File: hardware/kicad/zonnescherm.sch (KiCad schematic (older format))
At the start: 28 parts, among them K1 K1-ON/OFF, K2 K1-UP/DOWN, K3 K2-ON/OFF, K4 K2-UP/DOWN, P1 ARDUINO-ISP, P2 CONN_MAINS, P3 CONN_SUNSHADE1, P4 CONN_SUNSHADE2, SW1 SW_UP_1, SW2 SW_DOWN_1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

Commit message: Updated PCB
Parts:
- removed SW1: SW_UP_1, Buttons_Switches_ThroughHole:SW_PUSH_SMALL, symbol SW_PUSH
- removed SW2: SW_DOWN_1, Buttons_Switches_ThroughHole:SW_PUSH_SMALL, symbol SW_PUSH
- removed SW3: SW_UP_2, Buttons_Switches_ThroughHole:SW_PUSH_SMALL, symbol SW_PUSH
- removed SW4: SW_DOWN_2, Buttons_Switches_ThroughHole:SW_PUSH_SMALL, symbol SW_PUSH
- added C5: 100n, Capacitors_SMD:C_0805_HandSoldering, symbol C
- added P5: CONN_02X04, Pin_Headers:Pin_Header_Straight_2x04, symbol CONN_02X04
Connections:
- wire segments 123 -> 134
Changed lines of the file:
@@
-$EndComp
-$Comp
-L SW_PUSH SW1
-U 1 1 57852FF2
-P 1800 4750
-F 0 "SW1" H 1950 4860 50  0000 C CNN
-F 1 "SW_UP_1" H 1800 4670 50  0000 C CNN
-F 2 "Buttons_Switches_ThroughHole:SW_PUSH_SMALL" H 1800 4750 50  0001 C CNN
-F 3 "" H 1800 4750 50  0000 C CNN
-	1    1800 4750
-	1    0    0    -1
-$EndComp
-$Comp
-L SW_PUSH SW2
-U 1 1 57853071
-P 1800 5050
-F 0 "SW2" H 1950 5160 50  0000 C CNN
-F 1 "SW_DOWN_1" H 1800 4970 50  0000 C CNN
-F 2 "Buttons_Switches_ThroughHole:SW_PUSH_SMALL" H 1800 5050 50  0001 C CNN
-F 3 "" H 1800 5050 50  0000 C CNN
-	1    1800 5050
-	1    0    0    -1
-$EndComp
-$Comp
-L SW_PUSH SW3
-U 1 1 57853154
-P 1800 5350
-F 0 "SW3" H 1950 5460 50  0000 C CNN
-F 1 "SW_UP_2" H 1800 5270 50  0000 C CNN
-F 2 "Buttons_Switches_ThroughHole:SW_PUSH_SMALL" H 1800 5350 50  0001 C CNN
-F 3 "" H 1800 5350 50  0000 C CNN
-	1    1800 5350
-	1    0    0    -1
-$EndComp
-$Comp
-L SW_PUSH SW4
-U 1 1 57853197
-P 1800 5650
-F 0 "SW4" H 1950 5760 50  0000 C CNN
-F 1 "SW_DOWN_2" H 1800 5570 50  0000 C CNN
-F 2 "Buttons_Switches_ThroughHole:SW_PUSH_SMALL" H 1800 5650 50  0001 C CNN
-F 3 "" H 1800 5650 50  0000 C CNN
-	1    1800 5650
-	1    0    0    -1
 $EndComp
 $Comp
@@
 XRES
 Wire Wire Line
-	1500 4750 1350 4750
+	1350 4750 1550 4750
 Wire Wire Line
 	1350 4750 1350 5800
-Wire Wire Line
-	1350 5650 1500 5650
-Wire Wire Line
-	1500 5350 1350 5350
-Connection ~ 1350 5350
-Wire Wire Line
-	1500 5050 1350 5050
-Connection ~ 1350 5050
-Connection ~ 1350 5650
 $Comp
 L GND #PWR05
@@
 $EndComp
 Wire Wire Line
-	2100 4750 2300 4750
-Wire Wire Line
-	2100 5350 2300 5350
-Wire Wire Line
-	2100 5650 2300 5650
-Wire Wire Line
-	2100 5050 2300 5050
+	2050 4750 2300 4750
 $Comp
 L GND #PWR06
@@
 	1    0    0    -1
 $EndComp
+Text GLabel 2300 5050 2    60   Output ~ 0
+GPIO0
+Text GLabel 2300 5200 2    60   Output ~ 0
+GPIO2
 Text GLabel 2300 4750 2    60   Output ~ 0
-GPIO0
-Text GLabel 2300 5050 2    60   Output ~ 0
-GPIO2
-Text GLabel 2300 5350 2    60   Output ~ 0
 GPIO5
-Text GLabel 2300 5650 2    60   Output ~ 0
+Text GLabel 2300 4900 2    60   Output ~ 0
 GPIO4
 Text GLabel 5300 3800 2    60   Input ~ 0
@@
 Wire Wire Line
 	5950 5650 5700 5650
+$Comp
+L CONN_02X04 P5
+U 1 1 5790E325
+P 1800 4900
+F 0 "P5" H 1800 5150 50  0000 C CNN
+F 1 "CONN_02X04" H 1800 4650 50  0000 C CNN
+F 2 "Pin_Headers:Pin_Header_Straight_2x04" H 1800 3700 50  0001 C CNN
+F 3 "" H 1800 3700 50  0000 C CNN
+	1    1800 4900
+	1    0    0    -1
+$EndComp
+Wire Wire Line
+	1550 4850 1350 4850
+Connection ~ 1350 4850
+Wire Wire Line
+	1550 4950 1350 4950
+Connection ~ 1350 4950
+Wire Wire Line
+	1550 5050 1350 5050
+Connection ~ 1350 5050
+Wire Wire Line
+	2050 4850 2200 4850
+Wire Wire Line
+	2200 4850 2200 4900
+Wire Wire Line
+	2200 4900 2300 4900
+Wire Wire Line
+	2050 4950 2200 4950
+Wire Wire Line
+	2200 4950 2200 5050
+Wire Wire Line
+	2200 5050 2300 5050
+Wire Wire Line
+	2050 5050 2150 5050
+Wire Wire Line
+	2150 5050 2150 5200
+Wire Wire Line
+	2150 5200 2300 5200
+$Comp
+L C C5
+U 1 1 5790FD2E
+P 3100 5200
+F 0 "C5" H 3125 5300 50  0000 L CNN
+F 1 "100n" H 3125 5100 50  0000 L CNN
+F 2 "Capacitors_SMD:C_0805_HandSoldering" H 3138 5050 50  0001 C CNN
+F 3 "" H 3100 5200 50  0000 C CNN
+	1    3100 5200
+	1    0    0    -1
+$EndComp
+$Comp
+L GND #PWR09
+U 1 1 5790FDB2
+P 3100 5450
+F 0 "#PWR09" H 3100 5200 50  0001 C CNN
+F 1 "GND" H 3100 5300 50  0000 C CNN
+F 2 "" H 3100 5450 50  0000 C CNN
+F 3 "" H 3100 5450 50  0000 C CNN
+	1    3100 5450
+	1    0    0    -1
+$EndComp
+Wire Wire Line
+	3100 5450 3100 5350
+Wire Wire Line
+	3100 5050 3100 4950
+Wire Wire Line
+	3100 4950 3300 4950
+Text GLabel 3300 4950 2    60   Output ~ 0
+P5V
+Wire Wire Line
+	10350 2000 10200 2000
+Wire Wire Line
+	10200 2000 10200 1900
+Connection ~ 10200 1900
 $EndSCHEMATC

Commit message: Added logo
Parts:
- P5: value CONN_02X04 -> SWITCHES
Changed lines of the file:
@@
 P 1800 4900
 F 0 "P5" H 1800 5150 50  0000 C CNN
-F 1 "CONN_02X04" H 1800 4650 50  0000 C CNN
+F 1 "SWITCHES" H 1800 4650 50  0000 C CNN
 F 2 "Pin_Headers:Pin_Header_Straight_2x04" H 1800 3700 50  0001 C CNN
 F 3 "" H 1800 3700 50  0000 C CNN

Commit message: Updated layout, added text etc.
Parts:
- C1: footprint Capacitors_SMD:c_elec_5x5.3 -> Capacitors_SMD:c_elec_8x6.5
- C4: footprint Capacitors_SMD:c_elec_5x5.3 -> Capacitors_SMD:c_elec_4x5.8
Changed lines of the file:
@@
 F 0 "C4" H 5025 1950 50  0000 L CNN
 F 1 "10u/16V" H 5025 1750 50  0000 L CNN
-F 2 "Capacitors_SMD:c_elec_5x5.3" H 5038 1700 50  0001 C CNN
+F 2 "Capacitors_SMD:c_elec_4x5.8" H 5038 1700 50  0001 C CNN
 F 3 "" H 5000 1850 50  0000 C CNN
 	1    5000 1850
@@
 F 0 "C1" H 3575 1950 50  0000 L CNN
 F 1 "100u/16V" H 3575 1750 50  0000 L CNN
-F 2 "Capacitors_SMD:c_elec_5x5.3" H 3588 1700 50  0001 C CNN
+F 2 "Capacitors_SMD:c_elec_8x6.5" H 3588 1700 50  0001 C CNN
 F 3 "" H 3550 1850 50  0000 C CNN
 	1    3550 1850

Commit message: Added high voltage logo
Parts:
- added C6, C7: 100n, Capacitors_SMD:C_0805_HandSoldering, symbol C
- added R8: 390, Resistors_SMD:R_0805_HandSoldering, symbol R
- P5: footprint Pin_Headers:Pin_Header_Straight_2x04 -> Pin_Headers:Pin_Header_Straight_2x05; symbol CONN_02X04 -> CONN_02X05
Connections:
- net GND: now also P5.9 (P9), C6.2, C7.2
- net P3V3: now also C7.1, R8.2
- net P5V: now also C6.1
- new net: P5.10 (P10), R8.1
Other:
- moved on the sheet: C2, C3
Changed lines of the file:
@@
 L C C3
 U 1 1 578534E0
-P 4400 5200
-F 0 "C3" H 4425 5300 50  0000 L CNN
-F 1 "100n" H 4425 5100 50  0000 L CNN
-F 2 "Capacitors_SMD:C_0805_HandSoldering" H 4438 5050 50  0001 C CNN
-F 3 "" H 4400 5200 50  0000 C CNN
-	1    4400 5200
+P 4700 5200
+F 0 "C3" H 4725 5300 50  0000 L CNN
+F 1 "100n" H 4725 5100 50  0000 L CNN
+F 2 "Capacitors_SMD:C_0805_HandSoldering" H 4738 5050 50  0001 C CNN
+F 3 "" H 4700 5200 50  0000 C CNN
+	1    4700 5200
 	1    0    0    -1
 $EndComp
@@
 L C C2
 U 1 1 57853591
-P 3750 5200
-F 0 "C2" H 3775 5300 50  0000 L CNN
-F 1 "100n" H 3775 5100 50  0000 L CNN
-F 2 "Capacitors_SMD:C_0805_HandSoldering" H 3788 5050 50  0001 C CNN
-F 3 "" H 3750 5200 50  0000 C CNN
-	1    3750 5200
+P 4050 5200
+F 0 "C2" H 4075 5300 50  0000 L CNN
+F 1 "100n" H 4075 5100 50  0000 L CNN
+F 2 "Capacitors_SMD:C_0805_HandSoldering" H 4088 5050 50  0001 C CNN
+F 3 "" H 4050 5200 50  0000 C CNN
+	1    4050 5200
 	1    0    0    -1
 $EndComp
@@
 P3V3
 $Comp
-L GND #PWR01
+L GND #PWR8
 U 1 1 5785489F
 P 5000 2250
-F 0 "#PWR01" H 5000 2000 50  0001 C CNN
+F 0 "#PWR8" H 5000 2000 50  0001 C CNN
 F 1 "GND" H 5000 2100 50  0000 C CNN
 F 2 "" H 5000 2250 50  0000 C CNN
@@
 P3V3
 $Comp
-L GND #PWR02
+L GND #PWR9
 U 1 1 5785509B
 P 5450 4350
-F 0 "#PWR02" H 5450 4100 50  0001 C CNN
+F 0 "#PWR9" H 5450 4100 50  0001 C CNN
 F 1 "GND" H 5450 4200 50  0000 C CNN
 F 2 "" H 5450 4350 50  0000 C CNN
@@
 P3V3
 $Comp
-L GND #PWR03
+L GND #PWR1
 U 1 1 5787F342
 P 1150 4100
-F 0 "#PWR03" H 1150 3850 50  0001 C CNN
+F 0 "#PWR1" H 1150 3850 50  0001 C CNN
 F 1 "GND" H 1150 3950 50  0000 C CNN
 F 2 "" H 1150 4100 50  0000 C CNN
@@
 GPIO15
 $Comp
-L GND #PWR04
+L GND #PWR7
 U 1 1 5787FA28
-P 4400 5450
-F 0 "#PWR04" H 4400 5200 50  0001 C CNN
-F 1 "GND" H 4400 5300 50  0000 C CNN
-F 2 "" H 4400 5450 50  0000 C CNN
-F 3 "" H 4400 5450 50  0000 C CNN
-	1    4400 5450
-	1    0    0    -1
-$EndComp
-Wire Wire Line
-	4400 5050 4400 4950
-Wire Wire Line
-	4400 4950 4650 4950
-Wire Wire Line
-	4400 5350 4400 5450
-Text GLabel 4650 4950 2    60   Output ~ 0
+P 4700 5450
+F 0 "#PWR7" H 4700 5200 50  0001 C CNN
+F 1 "GND" H 4700 5300 50  0000 C CNN
+F 2 "" H 4700 5450 50  0000 C CNN
+F 3 "" H 4700 5450 50  0000 C CNN
+	1    4700 5450
+	1    0    0    -1
+$EndComp
+Wire Wire Line
+	4700 5050 4700 4950
+Wire Wire Line
+	4700 4950 4950 4950
+Wire Wire Line
+	4700 5350 4700 5450
+Text GLabel 4950 4950 2    60   Output ~ 0
 XRES
 Wire Wire Line
-	1350 4750 1550 4750
-Wire Wire Line
-	1350 4750 1350 5800
-$Comp
-L GND #PWR05
+	1350 6050 1550 6050
+Wire Wire Line
+	1350 6050 1350 7100
+$Comp
+L GND #PWR2
 U 1 1 5787FF4F
-P 1350 5800
-F 0 "#PWR05" H 1350 5550 50  0001 C CNN
-F 1 "GND" H 1350 5650 50  0000 C CNN
-F 2 "" H 1350 5800 50  0000 C CNN
-F 3 "" H 1350 5800 50  0000 C CNN
-	1    1350 5800
-	1    0    0    -1
-$EndComp
-Wire Wire Line
-	2050 4750 2300 4750
-$Comp
-L GND #PWR06
+P 1350 7100
+F 0 "#PWR2" H 1350 6850 50  0001 C CNN
+F 1 "GND" H 1350 6950 50  0000 C CNN
+F 2 "" H 1350 7100 50  0000 C CNN
+F 3 "" H 1350 7100 50  0000 C CNN
+	1    1350 7100
+	1    0    0    -1
+$EndComp
+Wire Wire Line
+	2050 6050 2300 6050
+$Comp
+L GND #PWR6
 U 1 1 57880BFE
-P 3750 5450
-F 0 "#PWR06" H 3750 5200 50  0001 C CNN
-F 1 "GND" H 3750 5300 50  0000 C CNN
-F 2 "" H 3750 5450 50  0000 C CNN
-F 3 "" H 3750 5450 50  0000 C CNN
-	1    3750 5450
-	1    0    0    -1
-$EndComp
-Wire Wire Line
-	3750 5050 3750 4950
-Wire Wire Line
-	3750 4950 3950 4950
-Wire Wire Line
-	3750 5350 3750 5450
-Text GLabel 3950 4950 2    60   Output ~ 0
+P 4050 5450
+F 0 "#PWR6" H 4050 5200 50  0001 C CNN
+F 1 "GND" H 4050 5300 50  0000 C CNN
+F 2 "" H 4050 5450 50  0000 C CNN
+F 3 "" H 4050 5450 50  0000 C CNN
+	1    4050 5450
+	1    0    0    -1
+$EndComp
+Wire Wire Line
+	4050 5050 4050 4950
+Wire Wire Line
+	3750 4950 4250 4950
+Wire Wire Line
+	4050 5350 4050 5450
+Text GLabel 4250 4950 2    60   Output ~ 0
 P3V3
 Wire Wire Line
@@
 Connection ~ 6100 4050
 $Comp
-L GND #PWR07
+L GND #PWR11
 U 1 1 578902F2
 P 6100 4350
-F 0 "#PWR07" H 6100 4100 50  0001 C CNN
+F 0 "#PWR11" H 6100 4100 50  0001 C CNN
 F 1 "GND" H 6100 4200 50  0000 C CNN
 F 2 "" H 6100 4350 50  0000 C CNN
@@
 	1    0    0    -1
 $EndComp
-Text GLabel 2300 5050 2    60   Output ~ 0
+Text GLabel 2300 6350 2    60   Output ~ 0
 GPIO0
-Text GLabel 2300 5200 2    60   Output ~ 0
+Text GLabel 2300 6500 2    60   Output ~ 0
 GPIO2
-Text GLabel 2300 4750 2    60   Output ~ 0
+Text GLabel 2300 6050 2    60   Output ~ 0
 GPIO5
-Text GLabel 2300 4900 2    60   Output ~ 0
+Text GLabel 2300 6200 2    60   Output ~ 0
 GPIO4
 Text GLabel 5300 3800 2    60   Input ~ 0
@@
 Connection ~ 1350 2800
 Wire Wire Line
-	10350 1900 10100 1900
+	10100 1900 10350 1900
 Wire Wire Line
 	7850 1900 9900 1900
@@
 $EndComp
 $Comp
-L GND #PWR08
+L GND #PWR10
 U 1 1 57893968
 P 5800 6150
-F 0 "#PWR08" H 5800 5900 50  0001 C CNN
+F 0 "#PWR10" H 5800 5900 50  0001 C CNN
 F 1 "GND" H 5800 6000 50  0000 C CNN
 F 2 "" H 5800 6150 50  0000 C CNN
@@
 	5950 5650 5700 5650
 $Comp
-L CONN_02X04 P5
+L CONN_02X05 P5
 U 1 1 5790E325
-P 1800 4900
-F 0 "P5" H 1800 5150 50  0000 C CNN
-F 1 "SWITCHES" H 1800 4650 50  0000 C CNN
-F 2 "Pin_Headers:Pin_Header_Straight_2x04" H 1800 3700 50  0001 C CNN
-F 3 "" H 1800 3700 50  0000 C CNN
-	1    1800 4900
-	1    0    0    -1
-$EndComp
-Wire Wire Line
-	1550 4850 1350 4850
-Connection ~ 1350 4850
-Wire Wire Line
-	1550 4950 1350 4950
-Connection ~ 1350 4950
-Wire Wire Line
-	1550 5050 1350 5050
-Connection ~ 1350 5050
-Wire Wire Line
-	2050 4850 2200 4850
-Wire Wire Line
-	2200 4850 2200 4900
-Wire Wire Line
-	2200 4900 2300 4900
-Wire Wire Line
-	2050 4950 2200 4950
-Wire Wire Line
-	2200 4950 2200 5050
-Wire Wire Line
-	2200 5050 2300 5050
-Wire Wire Line
-	2050 5050 2150 5050
-Wire Wire Line
-	2150 5050 2150 5200
-Wire Wire Line
-	2150 5200 2300 5200
+P 1800 6250
+F 0 "P5" H 1800 6550 50  0000 C CNN
+F 1 "SWITCHES" H 1800 5950 50  0000 C CNN
+F 2 "Pin_Headers:Pin_Header_Straight_2x05" H 1800 5050 50  0001 C CNN
+F 3 "" H 1800 5050 50  0000 C CNN
+	1    1800 6250
+	1    0    0    -1
+$EndComp
+Wire Wire Line
+	1550 6150 1350 6150
+Connection ~ 1350 6150
+Wire Wire Line
+	1550 6250 1350 6250
+Connection ~ 1350 6250
+Wire Wire Line
+	1550 6350 1350 6350
+Connection ~ 1350 6350
+Wire Wire Line
+	2050 6150 2200 6150
+Wire Wire Line
+	2200 6150 2200 6200
+Wire Wire Line
+	2200 6200 2300 6200
+Wire Wire Line
+	2050 6250 2200 6250
+Wire Wire Line
+	2200 6250 2200 6350
+Wire Wire Line
+	2200 6350 2300 6350
+Wire Wire Line
+	2050 6350 2150 6350
+Wire Wire Line
+	2150 6350 2150 6500
+Wire Wire Line
+	2150 6500 2300 6500
 $Comp
 L C C5
@@
 $EndComp
 $Comp
-L GND #PWR09
+L GND #PWR4
 U 1 1 5790FDB2
 P 3100 5450
-F 0 "#PWR09" H 3100 5200 50  0001 C CNN
+F 0 "#PWR4" H 3100 5200 50  0001 C CNN
 F 1 "GND" H 3100 5300 50  0000 C CNN
 F 2 "" H 3100 5450 50  0000 C CNN
@@
 	3100 5050 3100 4950
 Wire Wire Line
-	3100 4950 3300 4950
+	2800 4950 3300 4950
 Text GLabel 3300 4950 2    60   Output ~ 0
 P5V
@@
 	10200 2000 10200 1900
 Connection ~ 10200 1900
+Wire Wire Line
+	1550 6450 1350 6450
+Connection ~ 1350 6450
+Wire Wire Line
+	2050 6450 2050 6750
+Wire Wire Line
+	2050 6750 2300 6750
+Text GLabel 2800 6750 2    60   Output ~ 0
+P3V3
+$Comp
+L R R8
+U 1 1 579C55BD
+P 2450 6750
+F 0 "R8" V 2530 6750 50  0000 C CNN
+F 1 "390" V 2450 6750 50  0000 C CNN
+F 2 "Resistors_SMD:R_0805_HandSoldering" V 2380 6750 50  0001 C CNN
+F 3 "" H 2450 6750 50  0000 C CNN
+	1    2450 6750
+	0    -1   -1   0
+$EndComp
+Wire Wire Line
+	2600 6750 2800 6750
+$Comp
+L C C6
+U 1 1 579C5EFD
+P 2800 5200
+F 0 "C6" H 2825 5300 50  0000 L CNN
+F 1 "100n" H 2825 5100 50  0000 L CNN
+F 2 "Capacitors_SMD:C_0805_HandSoldering" H 2838 5050 50  0001 C CNN
+F 3 "" H 2800 5200 50  0000 C CNN
+	1    2800 5200
+	1    0    0    -1
+$EndComp
+$Comp
+L C C7
+U 1 1 579C5FA9
+P 3750 5200
+F 0 "C7" H 3775 5300 50  0000 L CNN
+F 1 "100n" H 3775 5100 50  0000 L CNN
+F 2 "Capacitors_SMD:C_0805_HandSoldering" H 3788 5050 50  0001 C CNN
+F 3 "" H 3750 5200 50  0000 C CNN
+	1    3750 5200
+	1    0    0    -1
+$EndComp
+Wire Wire Line
+	2800 5050 2800 4950
+Connection ~ 3100 4950
+Wire Wire Line
+	3750 5050 3750 4950
+Connection ~ 4050 4950
+$Comp
+L GND #PWR5
+U 1 1 579C61A4
+P 3750 5450
+F 0 "#PWR5" H 3750 5200 50  0001 C CNN
+F 1 "GND" H 3750 5300 50  0000 C CNN
+F 2 "" H 3750 5450 50  0000 C CNN
+F 3 "" H 3750 5450 50  0000 C CNN
+	1    3750 5450
+	1    0    0    -1
+$EndComp
+$Comp
+L GND #PWR3
+U 1 1 579C6206
+P 2800 5450
+F 0 "#PWR3" H 2800 5200 50  0001 C CNN
+F 1 "GND" H 2800 5300 50  0000 C CNN
+F 2 "" H 2800 5450 50  0000 C CNN
+F 3 "" H 2800 5450 50  0000 C CNN
+	1    2800 5450
+	1    0    0    -1
+$EndComp
+Wire Wire Line
+	2800 5450 2800 5350
+Wire Wire Line
+	3750 5450 3750 5350
 $EndSCHEMATC

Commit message: Updated the footprint and schematic symbol of the AC/DC converter module
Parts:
- U1: symbol IRM-05-5 -> IRM-05-5-RESCUE-zonnescherm
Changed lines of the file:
@@
 EESchema Schematic File Version 2
 LIBS:zonnescherm-rescue
-LIBS:power
-LIBS:device
-LIBS:transistors
-LIBS:conn
-LIBS:linear
-LIBS:regul
-LIBS:74xx
-LIBS:cmos4000
-LIBS:adc-dac
-LIBS:memory
-LIBS:xilinx
-LIBS:microcontrollers
-LIBS:dsp
-LIBS:microchip
-LIBS:analog_switches
-LIBS:motorola
-LIBS:texas
-LIBS:intel
-LIBS:audio
-LIBS:interface
-LIBS:digital-audio
-LIBS:philips
-LIBS:display
-LIBS:cypress
-LIBS:siliconi
-LIBS:opto
-LIBS:atmel
-LIBS:contrib
-LIBS:ESP8266
-LIBS:valves
 LIBS:modex
 LIBS:zonnescherm-cache
@@
 $EndComp
 $Comp
-L IRM-05-5 U1
+L IRM-05-5-RESCUE-zonnescherm U1
 U 1 1 57852A7E
 P 2700 1550

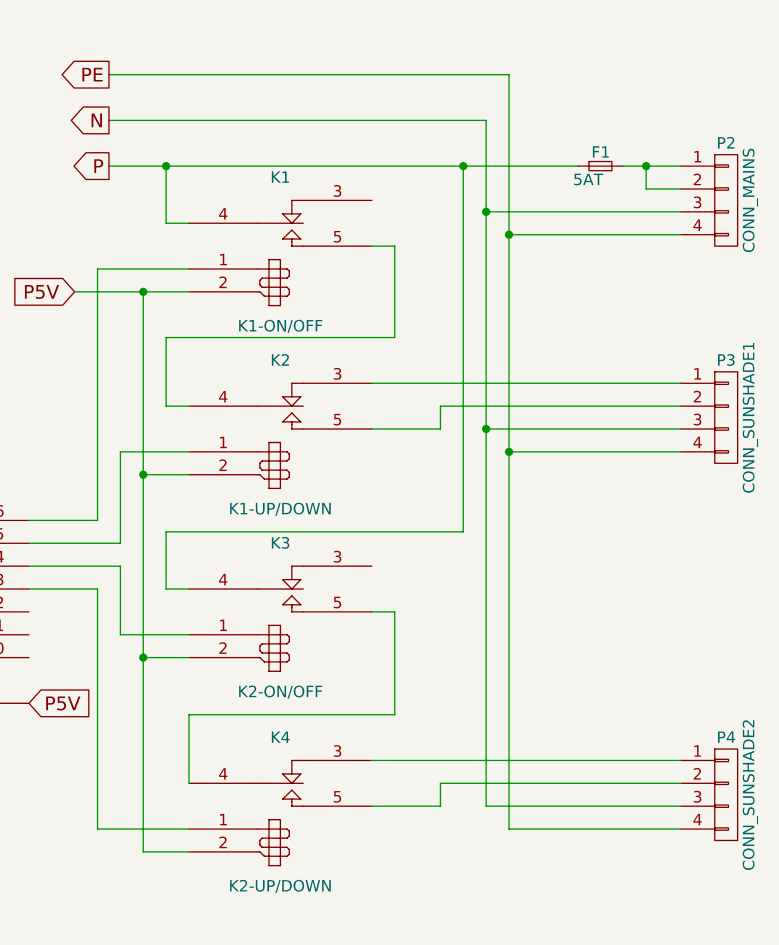
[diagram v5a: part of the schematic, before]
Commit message: Changed output configuration to enable global usage of the project.
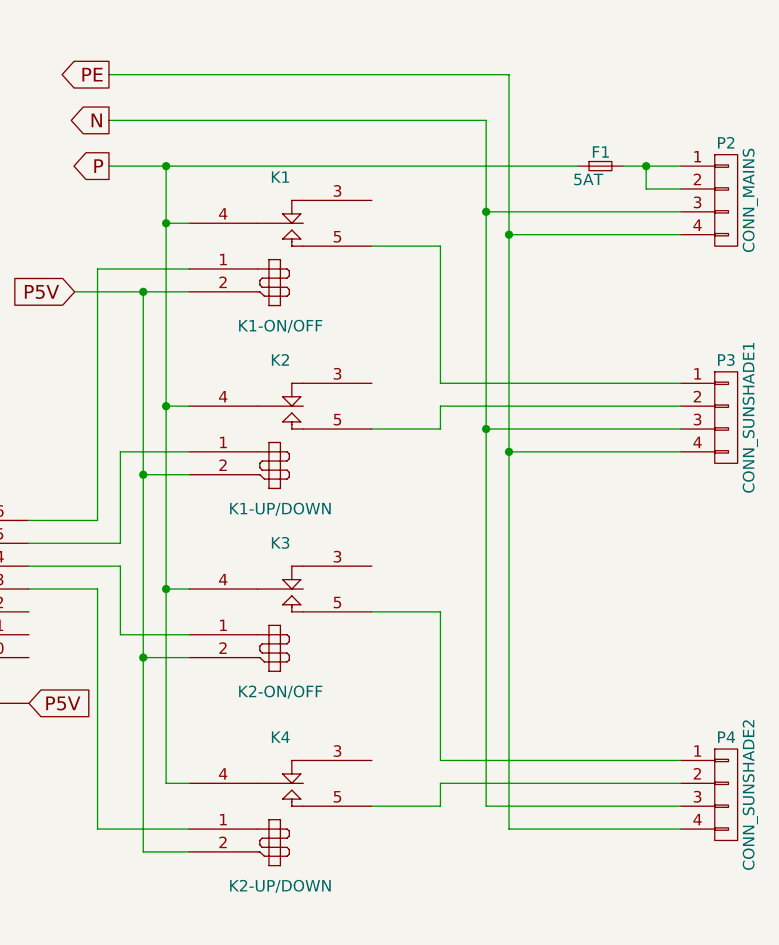
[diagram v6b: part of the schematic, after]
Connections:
- net P: now also K2.4 (C1), K4.4 (C1)
- net at K1.5 (T1): now also P3.1 (P1); no longer K2.4 (C1)
- net at K2.3 (R1): no longer P3.1 (P1)
- net at K3.5 (T1): now also P4.1 (P1); no longer K4.4 (C1)
- net at K4.3 (R1): no longer P4.1 (P1)
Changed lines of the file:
@@
-$EndComp
-$Comp
-L FTR-LYCA K2
-U 1 1 57852684
-P 8600 2900
-F 0 "K2" H 8600 3050 50  0000 C CNN
-F 1 "K1-UP/DOWN" H 8600 2400 50  0000 C CNN
-F 2 "modex:FTR_LY" H 8600 2900 50  0001 C CNN
-F 3 "" H 8600 2900 50  0000 C CNN
-	1    8600 2900
-	1    0    0    -1
 $EndComp
 $Comp
@@
 	7800 4800 8200 4800
 Wire Wire Line
-	8200 4600 8200 4300
-Wire Wire Line
-	8200 4300 9100 4300
-Wire Wire Line
-	9100 4300 9100 3850
-Wire Wire Line
-	9100 3850 9000 3850
-Wire Wire Line
-	8200 3750 8100 3750
-Wire Wire Line
-	8100 3750 8100 3500
-Wire Wire Line
-	8100 3500 9400 3500
-Wire Wire Line
-	9000 4500 10350 4500
-Wire Wire Line
 	9000 4700 9300 4700
 Wire Wire Line
-	8200 2950 8100 2950
-Wire Wire Line
-	8100 2950 8100 2650
-Wire Wire Line
-	8100 2650 9100 2650
-Wire Wire Line
-	9100 2650 9100 2250
-Wire Wire Line
-	9100 2250 9000 2250
-Wire Wire Line
 	8200 2150 8100 2150
 Wire Wire Line
-	8100 2150 8100 1900
-Wire Wire Line
-	9000 2850 10350 2850
+	8100 1900 8100 4600
 Wire Wire Line
 	9000 3050 9300 3050
@@
 	7850 1500 9600 1500
 Connection ~ 9600 2200
-Wire Wire Line
-	9400 3500 9400 1900
-Connection ~ 9400 1900
 Wire Wire Line
 	3050 2950 5800 2950
@@
 Wire Wire Line
 	3750 5450 3750 5350
+$Comp
+L FTR-LYCA K2
+U 1 1 57852684
+P 8600 2900
+F 0 "K2" H 8600 3050 50  0000 C CNN
+F 1 "K1-UP/DOWN" H 8600 2400 50  0000 C CNN
+F 2 "modex:FTR_LY" H 8600 2900 50  0001 C CNN
+F 3 "" H 8600 2900 50  0000 C CNN
+	1    8600 2900
+	1    0    0    -1
+$EndComp
+Wire Wire Line
+	8100 2950 8200 2950
+Connection ~ 8100 2150
+Wire Wire Line
+	8100 3750 8200 3750
+Connection ~ 8100 2950
+Wire Wire Line
+	8100 4600 8200 4600
+Connection ~ 8100 3750
+Wire Wire Line
+	10350 2850 9300 2850
+Wire Wire Line
+	9300 2850 9300 2250
+Wire Wire Line
+	9300 2250 9000 2250
+Wire Wire Line
+	9000 3850 9300 3850
+Wire Wire Line
+	9300 3850 9300 4500
+Wire Wire Line
+	9300 4500 10350 4500
 $EndSCHEMATC
